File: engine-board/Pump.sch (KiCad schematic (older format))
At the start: 13 parts, among them J1 Pump Controller, J301 Steering Turbines, J302 VL6180 Range Sensor, J303 Pump Current Sensor, J304 VL6180 Range Sensor, J305 Turbine 1 ESC, J306 Turbine 2 ESC, J307 Turbine Current Sensor, J308 Solenoid Current Sensor, J309 Solenoid, Q301 IRLB8721PBF

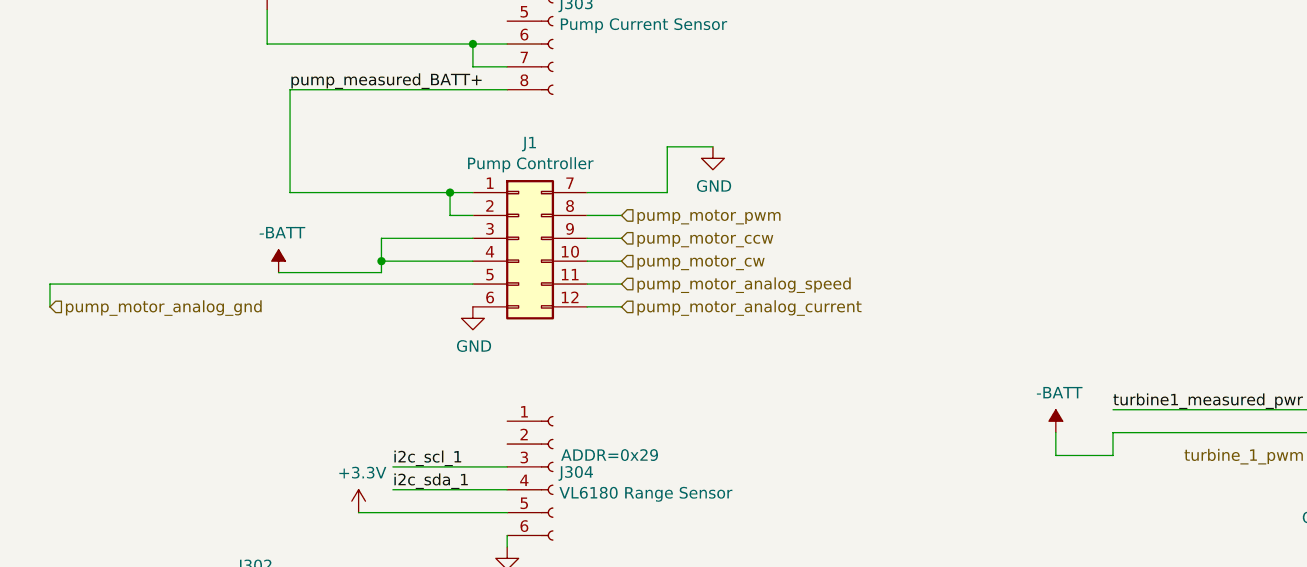
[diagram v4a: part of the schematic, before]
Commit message: board smaller
PCB V0.1 Errata:

- [QUESTION: - it looks like 12 on website] polulu 2814 has 16 pin footprint instead of 12...  AAACK!!!
- 5v and 3.3v traces could be wider
- [FIXED] fail: going into the power schematic scl + sda are swapped...
- [FIXED - moved to miniofit] pump controller silkscreen is wrong
- [FIXED] NOTE: just switch ALL to the minifit??
- [FIXED - will be on top, but not needed now] ADD: Ethernet connection from the teensy to the host computer board.
- [FIXED - going to use Qwiic) 9 Axis Mopak: wrong footprint - holes too small, spacing seems good, create outline as it bumps into feather header
- [FIXED] RV1805:  power + GND swapped... and I can’t seem to find them.
- [FIXED] 2 pressure sensors, the same i2c address... rerouted to 2nd i2c port on teensy
- [NOT NEEDED - adding display] Add RGB LED... it will be helpful for debugging.
- [FIXED - kindof - moved to micro-fit, might need to wire this directly to bulkhead] Turbine ferrules for power are 12 gauge - need bigger screw terminals if that is the connection method
- [FIXED] Feather footprint - lookup exactly what feather boards need for support..
- [FIXED] pump_motor_pwm is not connected to the TEENSY!!  blerg.  (jumper to pin 13 of feather for now)
- [FIXED - added FET] Maxon 70/30 POWER?  Think about power FET or ‘sleep’ to turn it off.
- [FIXED - added to bulkhead connector] Teensy 4.1 Program + ON/OFF pins - research how to extend these
- [TODO] remove VL6180 range sensor
- [LATER - will add to cost.. possibly remove?] put battery on back side
- add silkscreen for polulu
- [FIXED] Reorganize connectors:
    - Pump motor connectors go on end - attached in closing
    - bulkhead connectors go on side as they will always be attached
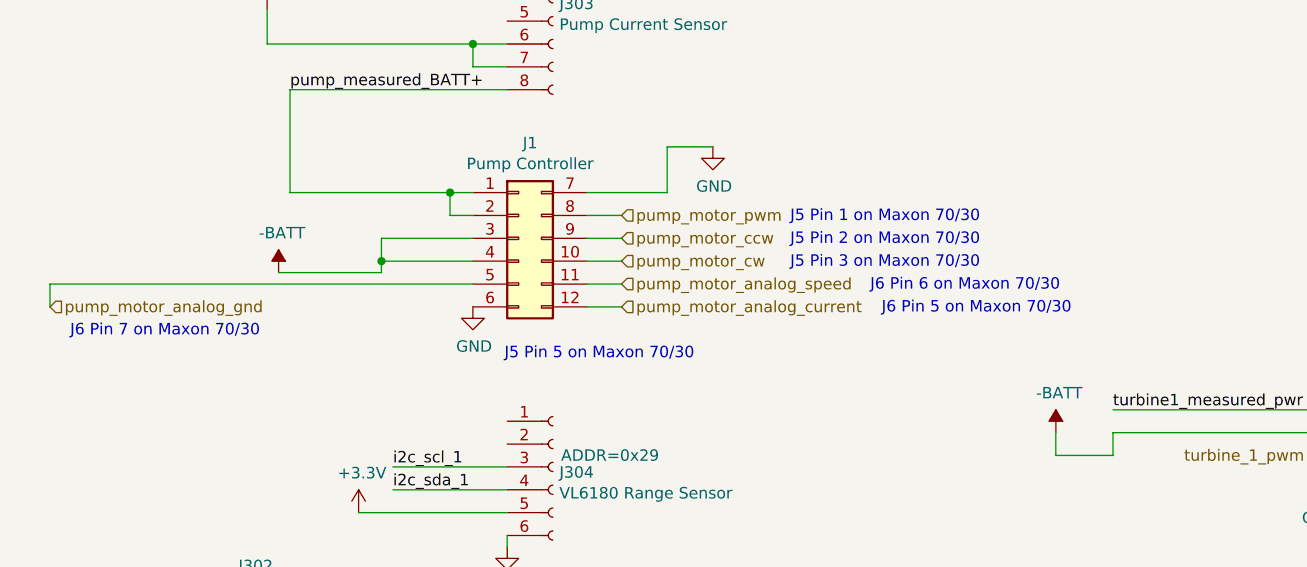
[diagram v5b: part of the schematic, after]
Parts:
- D301: Link (none) -> https://www.digikey.com/en/products/detail/vishay-general-s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; MANUFACTURER (none) -> Vishay; Price (none) -> 0.52
- J1: footprint TerminalBlock_CUI:CUI_TBP01R1W-508-12BE -> Connector_Molex:Molex_Micro-Fit_3.0_43045-1221_2x06-1MP_P3.00mm_Horizontal
- J301: MANUFACTURER (none) -> Molex; MATE_Link (none) -> https://www.digikey.com/en/products/detail/molex/0430250800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; MATE_MPN (none) -> 430250800; MATE_Price (none) -> 0.6; MPM 0430450821 -> (none); MPN (none) -> 0430450821
- J302: Link2 (none) -> https://www.sparkfun.com/products/12785; MATE_Link https://www.digikey.com/en/products/detail/molex/0430250400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 -> https://www.digikey.com/en/products/detail/molex/0430250408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; MATE_MPN 430250400 -> 0430250408; MPN2 (none) -> SEN-12785; Manufacturer (none) -> Sparkfun; Price2 (none) -> 29.50
- J303: MATE_Link (none) -> https://www.digikey.com/en/products/detail/molex/0901210128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; MATE_MPN (none) -> 0901210128; MATE_Price (none) -> 1.16
- J305, J306: footprint TerminalBlock_CUI:CUI_TBP01R1W-508-08BE -> Connector_Molex:Molex_Micro-Fit_3.0_43045-0821_2x04-1MP_P3.00mm_Horizontal; Link2 (none) -> https://bluerobotics.com/store/thrusters/speed-controllers/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; MATE_Link (none) -> https://www.digikey.com/en/products/detail/cui-devices/TBP0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; MATE_MPN (none) -> TBP01P1W-508-08BE; MATE_Price (none) -> 2.54; MPN2 (none) -> BESC30-R3; Manufacturer (none) -> Blue Robotics; Price2 (none) -> 30
- J307, J308: Link https://www.digikey.com/en/products/detail/samtec-inc/SSQ-106-01-G-S/1110613 -> https://www.digikey.com/en/products/detail/samtec-inc/SSQ-108-01-G-S/1110611; MATE_Link (none) -> https://www.digikey.com/en/products/detail/molex/0901210128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; MATE_MPN (none) -> 0901210128; MATE_Price (none) -> 1.16; Manufacturer (none) -> Adafruit
- J309: footprint TerminalBlock_CUI:CUI_TBP01R1W-508-02BE -> Connector_Molex:Molex_Micro-Fit_3.0_43045-0221_2x01-1MP_P3.00mm_Horizontal; Link2 (none) -> https://www.gghyd.com/valves/solenoid-valves/2-way/normally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; MATE_Link (none) -> https://www.digikey.com/en/products/detail/cui-devices/TBP0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; MATE_MPN (none) -> TBP01P1W-508-02BE; MATE_Price (none) -> 1.17; MPN2 (none) -> 20CC02LV7B7A; Manufacturer (none) -> Parker; Price2 (none) -> 125.0
- Q301: MANUFACTURER Infineon -> (none); MPN IRLB8721PBF -> IRLZ44NPBF; Manufacturer (none) -> Infineon
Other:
- note added: "J5 Pin 1 on Maxon 70/30"
- note added: "J5 Pin 2 on Maxon 70/30"
- note added: "J5 Pin 3 on Maxon 70/30"
- note added: "J5 Pin 5 on Maxon 70/30"
- note added: "J6 Pin 5 on Maxon 70/30"
- note added: "J6 Pin 6 on Maxon 70/30"
- note added: "J6 Pin 7 on Maxon 70/30"
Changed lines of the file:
@@
 F 1 "IRLB8721PBF" H 8354 1255 50  0000 L CNN
 F 2 "Package_TO_SOT_THT:TO-220-3_Vertical" H 8400 1225 50  0001 L CIN
-F 3 "http://www.infineon.com/dgdl/irlb8721pbf.pdf?fileId=5546d462533600a40153566056732591" H 8150 1300 50  0001 L CNN
+F 3 "" H 8150 1300 50  0001 L CNN
 F 4 "https://www.digikey.com/en/products/detail/infineon-technologies/IRLB8721PBF/2127670" H 8150 1300 50  0001 C CNN "Link"
-F 5 "Infineon" H 8150 1300 50  0001 C CNN "MANUFACTURER"
-F 6 "IRLB8721PBF" H 8150 1300 50  0001 C CNN "MPN"
+F 5 "" H 8150 1300 50  0001 C CNN "MANUFACTURER"
+F 6 "IRLZ44NPBF" H 8150 1300 50  0001 C CNN "MPN"
 F 7 "1.08" H 8150 1300 50  0001 C CNN "Price"
+F 8 "Infineon" H 8150 1300 50  0001 C CNN "Manufacturer"
 	1    8150 1300
 	1    0    0    -1
@@
 F 2 "Diode_THT:D_DO-41_SOD81_P10.16mm_Horizontal" H 9050 1325 50  0001 C CNN
 F 3 "http://www.vishay.com/docs/88503/1n4001.pdf" H 9050 1500 50  0001 C CNN
+F 4 "https://www.digikey.com/en/products/detail/vishay-general-semiconductor-diodes-division/1N4001GP-E3-54/2142384" H 9050 1500 50  0001 C CNN "Link"
+F 5 "Vishay" H 9050 1500 50  0001 C CNN "MANUFACTURER"
+F 6 "0.52" H 9050 1500 50  0001 C CNN "Price"
 	1    9050 1500
 	1    0    0    -1
@@
 F 0 "J309" H 9428 1476 50  0000 L CNN
 F 1 "Solenoid" H 9428 1385 50  0000 L CNN
-F 2 "TerminalBlock_CUI:CUI_TBP01R1W-508-02BE" H 9400 1500 50  0001 C CNN
+F 2 "Connector_Molex:Molex_Micro-Fit_3.0_43045-0221_2x01-1MP_P3.00mm_Horizontal" H 9400 1500 50  0001 C CNN
 F 3 "~" H 9400 1500 50  0001 C CNN
 F 4 "https://www.digikey.com/en/products/detail/cui-devices/TBP01R1W-508-02BE/10238425" H 9400 1500 50  0001 C CNN "Link"
@@
 F 6 "TBP01R1W-508-02BE" H 9400 1500 50  0001 C CNN "MPN"
 F 7 "0.77" H 9400 1500 50  0001 C CNN "Price"
+F 8 "https://www.gghyd.com/valves/solenoid-valves/2-way/normally-closed/stainless-steel/air-water-steam-or-oil/20cc02lv7b7a-parker-g7-2-way-normally-closed-1-8-npt-direct-acting-stainless-steel-solenoid-valve.html" H 9400 1500 50  0001 C CNN "Link2"
+F 9 "20CC02LV7B7A" H 9400 1500 50  0001 C CNN "MPN2"
+F 10 "Parker" H 9400 1500 50  0001 C CNN "Manufacturer"
+F 11 "125.0" H 9400 1500 50  0001 C CNN "Price2"
+F 12 "https://www.digikey.com/en/products/detail/cui-devices/TBP01P1W-508-02BE/10238415" H 9400 1500 50  0001 C CNN "MATE_Link"
+F 13 "TBP01P1W-508-02BE" H 9400 1500 50  0001 C CNN "MATE_MPN"
+F 14 "1.17" H 9400 1500 50  0001 C CNN "MATE_Price"
 	1    9400 1500
 	1    0    0    -1
@@
 F 0 "J306" H 6700 4867 50  0000 C CNN
 F 1 "Turbine 2 ESC" H 6700 4776 50  0000 C CNN
-F 2 "TerminalBlock_CUI:CUI_TBP01R1W-508-08BE" H 6650 4550 50  0001 C CNN
+F 2 "Connector_Molex:Molex_Micro-Fit_3.0_43045-0821_2x04-1MP_P3.00mm_Horizontal" H 6650 4550 50  0001 C CNN
 F 3 "~" H 6650 4550 50  0001 C CNN
 F 4 "https://www.digikey.com/en/products/detail/cui-devices/TBP01R1W-508-08BE/10238430" H 6650 4550 50  0001 C CNN "Link"
@@
 F 6 "TBP01R1W-508-08BE" H 6650 4550 50  0001 C CNN "MPN"
 F 7 "1.75" H 6650 4550 50  0001 C CNN "Price"
+F 8 "https://bluerobotics.com/store/thrusters/speed-controllers/besc30-r3/" H 6650 4550 50  0001 C CNN "Link2"
+F 9 "https://www.digikey.com/en/products/detail/cui-devices/TBP01P1W-508-08BE/10238420" H 6650 4550 50  0001 C CNN "MATE_Link"
+F 10 "TBP01P1W-508-08BE" H 6650 4550 50  0001 C CNN "MATE_MPN"
+F 11 "2.54" H 6650 4550 50  0001 C CNN "MATE_Price"
+F 12 "BESC30-R3" H 6650 4550 50  0001 C CNN "MPN2"
+F 13 "Blue Robotics" H 6650 4550 50  0001 C CNN "Manufacturer"
+F 14 "30" H 6650 4550 50  0001 C CNN "Price2"
 	1    6650 4550
 	1    0    0    -1
@@
 F 0 "J305" H 6700 4067 50  0000 C CNN
 F 1 "Turbine 1 ESC" H 6700 3976 50  0000 C CNN
-F 2 "TerminalBlock_CUI:CUI_TBP01R1W-508-08BE" H 6650 3750 50  0001 C CNN
+F 2 "Connector_Molex:Molex_Micro-Fit_3.0_43045-0821_2x04-1MP_P3.00mm_Horizontal" H 6650 3750 50  0001 C CNN
 F 3 "~" H 6650 3750 50  0001 C CNN
 F 4 "https://www.digikey.com/en/products/detail/cui-devices/TBP01R1W-508-08BE/10238430" H 6650 3750 50  0001 C CNN "Link"
@@
 F 6 "TBP01R1W-508-08BE" H 6650 3750 50  0001 C CNN "MPN"
 F 7 "1.75" H 6650 3750 50  0001 C CNN "Price"
+F 8 "https://bluerobotics.com/store/thrusters/speed-controllers/besc30-r3/" H 6650 3750 50  0001 C CNN "Link2"
+F 9 "https://www.digikey.com/en/products/detail/cui-devices/TBP01P1W-508-08BE/10238420" H 6650 3750 50  0001 C CNN "MATE_Link"
+F 10 "TBP01P1W-508-08BE" H 6650 3750 50  0001 C CNN "MATE_MPN"
+F 11 "2.54" H 6650 3750 50  0001 C CNN "MATE_Price"
+F 12 "BESC30-R3" H 6650 3750 50  0001 C CNN "MPN2"
+F 13 "Blue Robotics" H 6650 3750 50  0001 C CNN "Manufacturer"
+F 14 "30" H 6650 3750 50  0001 C CNN "Price2"
 	1    6650 3750
 	1    0    0    -1
@@
 F 3 "~" H 2900 5350 50  0001 C CNN
 F 4 "https://www.digikey.com/short/zjp71dn8" H 2900 5350 50  0001 C CNN "Link"
-F 5 "0430450821" H 2900 5350 50  0001 C CNN "MPM"
+F 5 "0430450821" H 2900 5350 50  0001 C CNN "MPN"
 F 6 "2.63" H 2900 5350 50  0001 C CNN "Price"
+F 7 "https://www.digikey.com/en/products/detail/molex/0430250800/252499" H 2900 5350 50  0001 C CNN "MATE_Link"
+F 8 "430250800" H 2900 5350 50  0001 C CNN "MATE_MPN"
+F 9 "0.6" H 2900 5350 50  0001 C CNN "MATE_Price"
+F 10 "Molex" H 2900 5350 50  0001 C CNN "MANUFACTURER"
 	1    2900 5350
 	1    0    0    -1
@@
 F 2 "Connector_PinSocket_2.54mm:PinSocket_1x08_P2.54mm_Vertical" H 6900 5500 50  0001 C CNN
 F 3 "~" H 6900 5500 50  0001 C CNN
-F 4 "https://www.digikey.com/en/products/detail/samtec-inc/SSQ-106-01-G-S/1110613" H 6900 5500 50  0001 C CNN "Link"
+F 4 "https://www.digikey.com/en/products/detail/samtec-inc/SSQ-108-01-G-S/1110611" H 6900 5500 50  0001 C CNN "Link"
 F 5 "Samtec Inc." H 6900 5500 50  0001 C CNN "MANUFACTURER"
 F 6 "SSQ-108-01-G-S" H 6900 5500 50  0001 C CNN "MPN"
@@
 F 9 "https://www.adafruit.com/product/4226" H 6900 5500 50  0001 C CNN "Link2"
 F 10 "ADDR=0x45" H 7150 5550 50  0000 C CNN "I2C_ADDR"
+F 11 "https://www.digikey.com/en/products/detail/molex/0901210128/760817?s=N4IgTCBcDaIJwAYCMYnLADhAXQL5A" H 6900 5500 50  0001 C CNN "MATE_Link"
+F 12 "0901210128" H 6900 5500 50  0001 C CNN "MATE_MPN"
+F 13 "1.16" H 6900 5500 50  0001 C CNN "MATE_Price"
+F 14 "Adafruit" H 6900 5500 50  0001 C CNN "Manufacturer"
 	1    6900 5500
 	1    0    0    -1
@@
 F 2 "Connector_PinSocket_2.54mm:PinSocket_1x08_P2.54mm_Vertical" H 9000 2400 50  0001 C CNN
 F 3 "~" H 9000 2400 50  0001 C CNN
-F 4 "https://www.digikey.com/en/products/detail/samtec-inc/SSQ-106-01-G-S/1110613" H 9000 2400 50  0001 C CNN "Link"
+F 4 "https://www.digikey.com/en/products/detail/samtec-inc/SSQ-108-01-G-S/1110611" H 9000 2400 50  0001 C CNN "Link"
 F 5 "Samtec Inc." H 9000 2400 50  0001 C CNN "MANUFACTURER"
 F 6 "SSQ-108-01-G-S" H 9000 2400 50  0001 C CNN "MPN"
@@
 F 9 "https://www.adafruit.com/product/4226" H 9000 2400 50  0001 C CNN "Link2"
 F 10 "ADDR=0x42" H 9250 2450 50  0000 C CNN "I2C_ADDR"
+F 11 "https://www.digikey.com/en/products/detail/molex/0901210128/760817?s=N4IgTCBcDaIJwAYCMYnLADhAXQL5A" H 9000 2400 50  0001 C CNN "MATE_Link"
+F 12 "0901210128" H 9000 2400 50  0001 C CNN "MATE_MPN"
+F 13 "1.16" H 9000 2400 50  0001 C CNN "MATE_Price"
+F 14 "Adafruit" H 9000 2400 50  0001 C CNN "Manufacturer"
 	1    9000 2400
 	1    0    0    -1
@@
 F 9 "https://www.adafruit.com/product/4226" H 3100 1850 50  0001 C CNN "Link2"
 F 10 "ADDR=0x43" H 3350 1900 50  0000 C CNN "I2C_ADDR"
+F 11 "https://www.digikey.com/en/products/detail/molex/0901210128/760817?s=N4IgTCBcDaIJwAYCMYnLADhAXQL5A" H 3100 1850 50  0001 C CNN "MATE_Link"
+F 12 "0901210128" H 3100 1850 50  0001 C CNN "MATE_MPN"
+F 13 "1.16" H 3100 1850 50  0001 C CNN "MATE_Price"
 	1    3100 1850
 	1    0    0    -1
@@
 F 6 "0430450422" H 1750 4550 50  0001 C CNN "MPN"
 F 7 "2.38" H 1750 4550 50  0001 C CNN "Price"
-F 8 "430250400" H 1750 4550 50  0001 C CNN "MATE_MPN"
+F 8 "0430250408" H 1750 4550 50  0001 C CNN "MATE_MPN"
 F 9 "0.48" H 1750 4550 50  0001 C CNN "MATE_Price"
-F 10 "https://www.digikey.com/en/products/detail/molex/0430250400/252497" H 1750 4550 50  0001 C CNN "MATE_Link"
+F 10 "https://www.digikey.com/en/products/detail/molex/0430250408/4481508" H 1750 4550 50  0001 C CNN "MATE_Link"
+F 11 "https://www.sparkfun.com/products/12785" H 1750 4550 50  0001 C CNN "Link2"
+F 12 "SEN-12785" H 1750 4550 50  0001 C CNN "MPN2"
+F 13 "Sparkfun" H 1750 4550 50  0001 C CNN "Manufacturer"
+F 14 "29.50" H 1750 4550 50  0001 C CNN "Price2"
 	1    1750 4550
 	1    0    0    -1
@@
 F 0 "J1" H 3000 3317 50  0000 C CNN
 F 1 "Pump Controller" H 3000 3226 50  0000 C CNN
-F 2 "TerminalBlock_CUI:CUI_TBP01R1W-508-12BE" H 2950 2900 50  0001 C CNN
+F 2 "Connector_Molex:Molex_Micro-Fit_3.0_43045-1221_2x06-1MP_P3.00mm_Horizontal" H 2950 2900 50  0001 C CNN
 F 3 "~" H 2950 2900 50  0001 C CNN
 F 4 "https://www.digikey.com/en/products/detail/cui-devices/TBP01R1W-508-12BE/10238432" H 2950 2900 50  0001 C CNN "Link"
@@
 	1    0    0    -1
 $EndComp
+Text Notes 4138 2936 0    50   ~ 0
+J5 Pin 2 on Maxon 70/30
+Text Notes 4138 3036 0    50   ~ 0
+J5 Pin 3 on Maxon 70/30
+Text Notes 4488 3136 0    50   ~ 0
+J6 Pin 6 on Maxon 70/30
+Text Notes 4538 3236 0    50   ~ 0
+J6 Pin 5 on Maxon 70/30
+Text Notes 988  3336 0    50   ~ 0
+J6 Pin 7 on Maxon 70/30
+Text Notes 4138 2836 0    50   ~ 0
+J5 Pin 1 on Maxon 70/30
+Text Notes 2888 3436 0    50   ~ 0
+J5 Pin 5 on Maxon 70/30
 $EndSCHEMATC
